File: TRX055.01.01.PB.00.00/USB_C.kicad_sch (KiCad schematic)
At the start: 3 parts, among them J9 1054500101

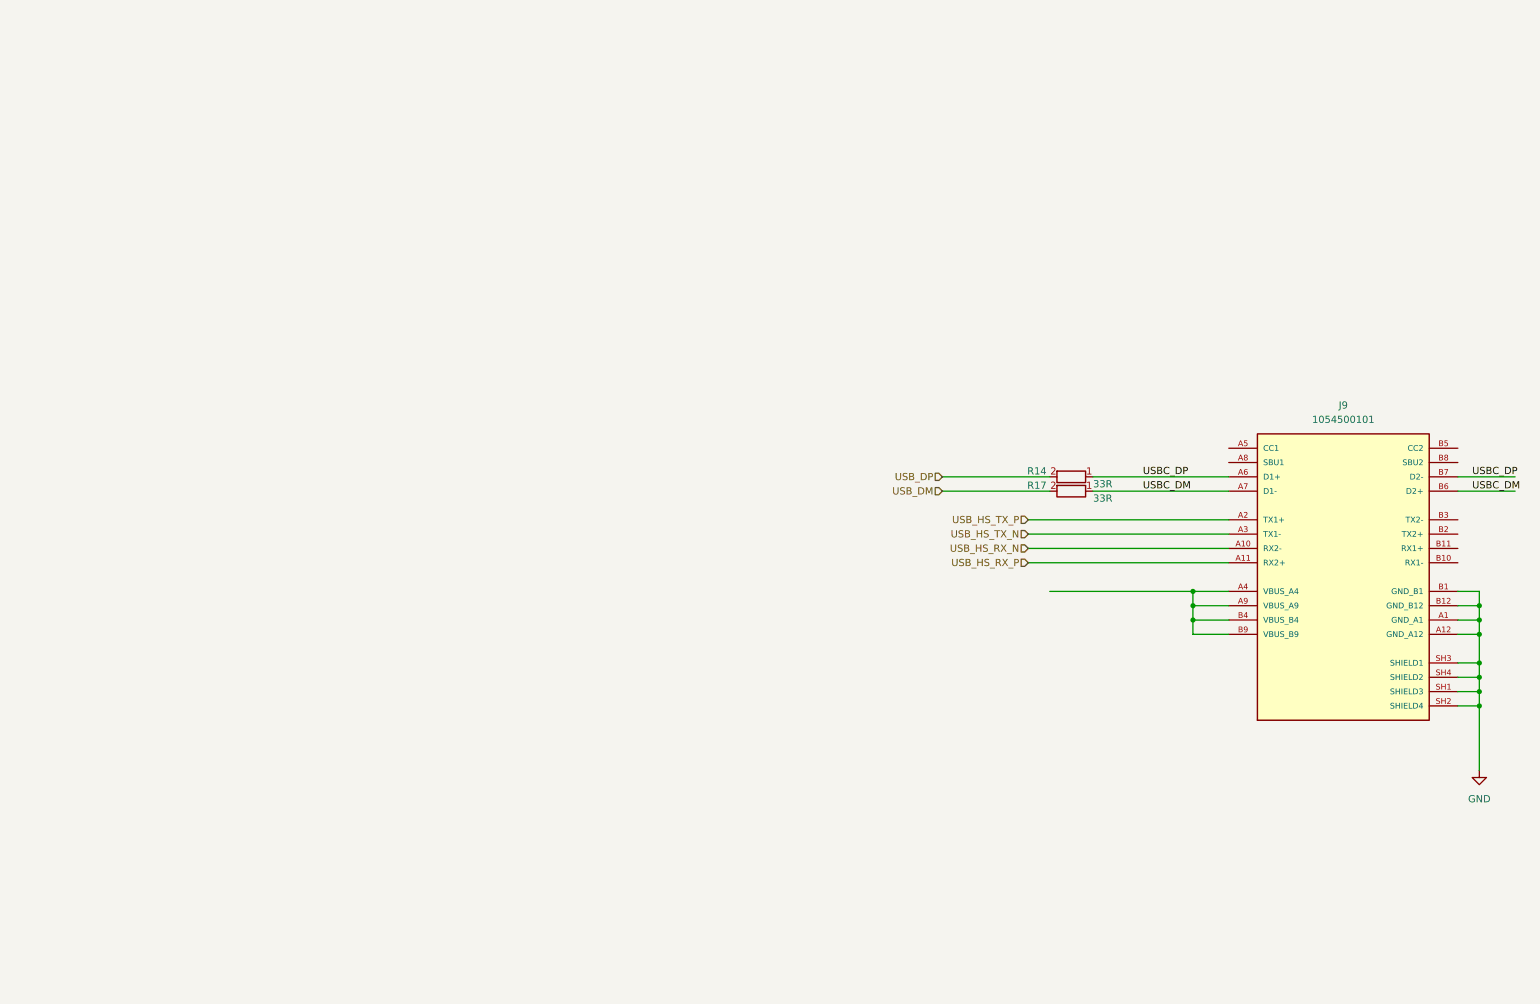
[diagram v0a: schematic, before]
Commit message: + add clocks + add PSU
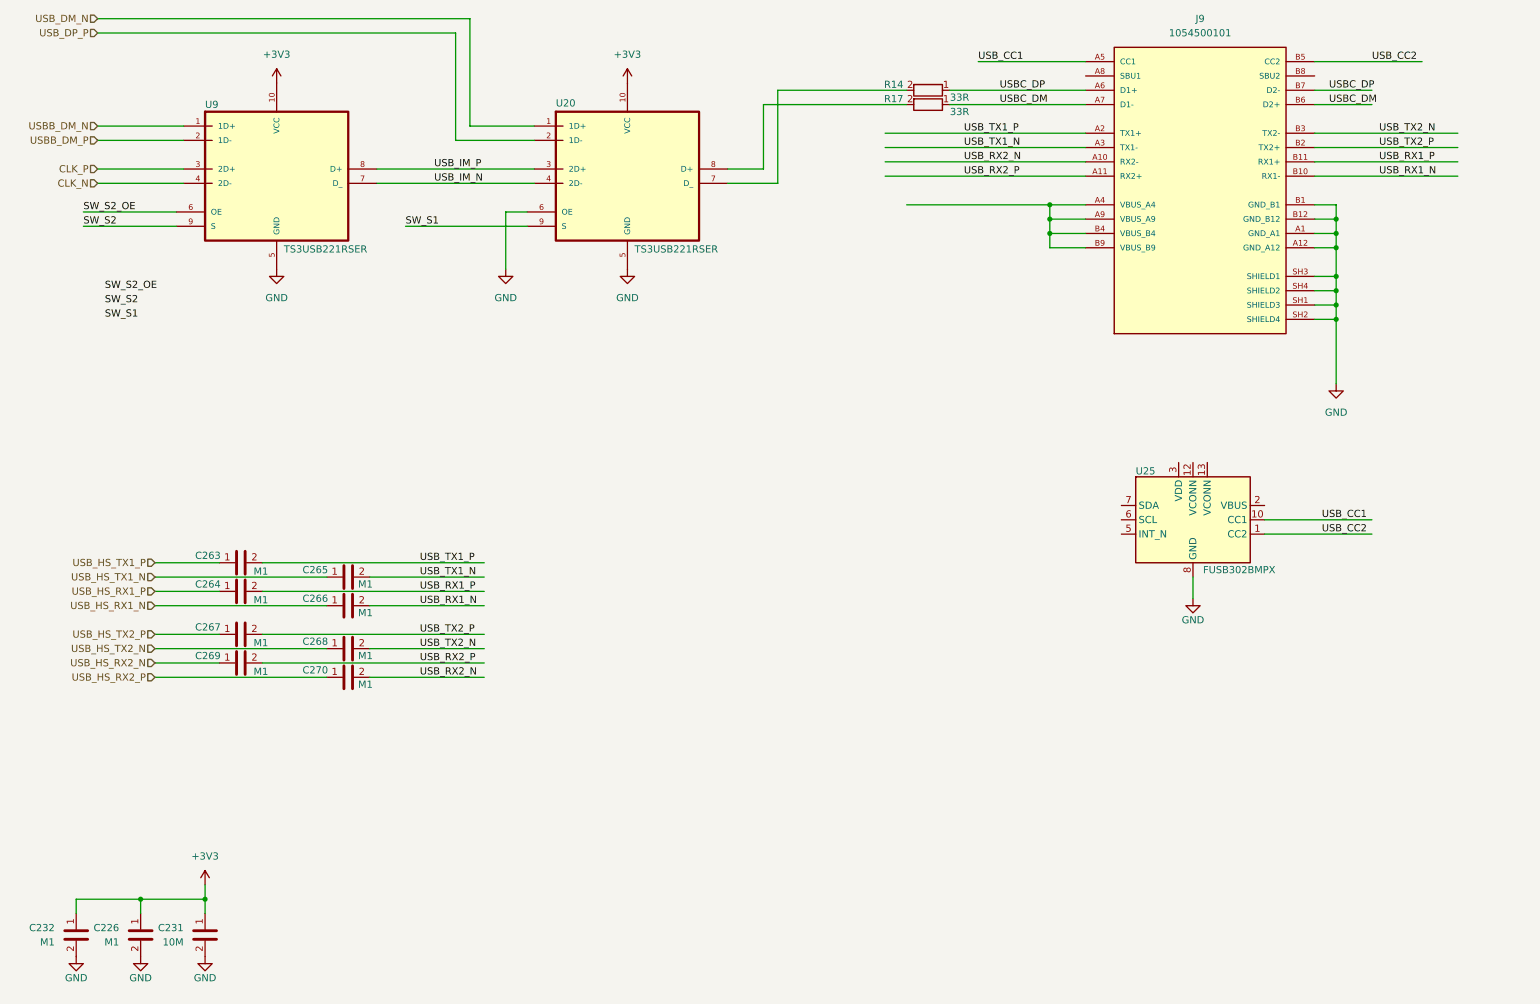
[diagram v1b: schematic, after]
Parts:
- added C226, C232, C263, C264, C265, C266, C267, C268, C269, C270: M1, Capacitor_SMD:C_0201_0603Metric, symbol PPA-Pasive:Cap
- added C231: 10M, Capacitor_SMD:C_0603_1608Metric, symbol PPA-Pasive:Cap
- added U20, U9: TS3USB221RSER, TS3USB221:IC_TPD6E001RSER, symbol TS3USB221:TS3USB221RSERG4
- added U25: FUSB302BMPX, Package_DFN_QFN:WQFN-14-1EP_2.5x2.5mm_P0.5mm_EP1.45x1.45mm, symbol Interface_USB:FUSB302BMPX
- J9: JLCPCB Part # (none) -> C134092
- R14, R17: JLCPCB Part # (none) -> C25105
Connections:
- net GND: now also C226.2, C231.2, C232.2, U20.5 (GND), U20.6 (OE), U25.15 (GND), U25.8 (GND), U25.9 (GND), U9.5 (GND)
- net USB_CC1: now reaches J9.A5 (CC1)
- net USB_CC1: now also U25.10 (CC1), U25.11 (CC1)
- net USB_RX1_N: now reaches J9.B10 (RX1-)
- net USB_RX1_N: now also C266.2
- net USB_RX1_P: now reaches J9.B11 (RX1+)
- net USB_RX1_P: now also C264.2
- net USB_TX2_P: now reaches J9.B2 (TX2+)
- net USB_TX2_P: now also C267.2
- net USB_TX2_N: now reaches J9.B3 (TX2-)
- net USB_TX2_N: now also C268.2
- net USB_CC2: now reaches J9.B5 (CC2)
- net USB_CC2: now also U25.1 (CC2), U25.14 (CC2)
- net USB_DM: no longer names the net of R17.2
- net USB_DM: now also U20.8 (D+)
- net USB_DP: no longer names the net of R14.2
- net USB_DP: now also U20.7 (D_)
- net USB_HS_RX_N renamed USB_RX2_N
- net USB_RX2_N: now also C270.2
- net USB_HS_RX_P renamed USB_RX2_P
- net USB_RX2_P: now also C269.2
- net USB_HS_TX_N renamed USB_TX1_N
- net USB_TX1_N: now also C265.2
- net USB_HS_TX_P renamed USB_TX1_P
- net USB_TX1_P: now also C263.2
- new net: U25.3 (VDD), U25.4 (VDD)
- new net +3V3: C226.1, C231.1, C232.1, U20.10 (VCC), U9.10 (VCC)
- new net CLK_N: U9.4 (2D-)
- new net CLK_P: U9.3 (2D+)
- new net SW_S1: U20.9 (S)
- new net SW_S2: U9.9 (S)
- new net SW_S2_OE: U9.6 (OE)
- new net USBB_DM_N: U9.1 (1D+)
- new net USBB_DM_P: U9.2 (1D-)
- new net USB_DM_N: U20.1 (1D+)
- new net USB_DP_P: U20.2 (1D-)
- new net USB_HS_RX1_N: C266.1
- new net USB_HS_RX1_P: C264.1
- new net USB_HS_RX2_N: C269.1
- new net USB_HS_RX2_P: C270.1
- new net USB_HS_TX1_N: C265.1
- new net USB_HS_TX1_P: C263.1
- new net USB_HS_TX2_N: C268.1
- new net USB_HS_TX2_P: C267.1
- new net USB_IM_N: U20.4 (2D-), U9.7 (D_)
- new net USB_IM_P: U20.3 (2D+), U9.8 (D+)
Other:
- moved on the sheet: J9, R14, R17

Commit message: V0.1 - production, added brig-up comments
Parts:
- added C275, C276, C277, C278: M1, Capacitor_SMD:C_0201_0603Metric, symbol PPA-Pasive:Cap
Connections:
- net +3V3: now also U25.3 (VDD), U25.4 (VDD), C275.2, C276.2, C277.2, C278.2
- net GND: now also C275.1, C276.1, C277.1, C278.1
- net VCONN: now reaches U25.12 (VCONN)
- net VCONN: now also U25.13 (VCONN)
- net USB_VBUS: now reaches U25.2 (VBUS)
- net USB_VBUS: now also J9.A4 (VBUS_A4), J9.A9 (VBUS_A9), J9.B4 (VBUS_B4), J9.B9 (VBUS_B9)
- net USB_CC_SCL: now reaches U25.6 (SCL)
- net USB_CC_SDA: now reaches U25.7 (SDA)
- net SW_S1 renamed USB_SW_S1
- net SW_S2 renamed USB_SW_S2
- net SW_S2_OE renamed USB_SW_S2_OE
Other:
- company: (none) -> Tronex s.r.o. / Tronex Group USA LLC
- title: (none) -> TRNX SDR Carrier board
- moved on the sheet: C263, C264, C265, C266, C267, C268, C269, C270, J9, R14, R17, U20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
